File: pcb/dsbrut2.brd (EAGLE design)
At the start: 51.6 x 38 mm, 13 parts, among them IC1 4175D, IC2 74HC125D, IC3 MEGA8-AI

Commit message: added fuse, fixed ic1 power supply with VSS
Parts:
- added L1: INDUCTOR-L1812, dp_devices:L1812
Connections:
- removed net VSS: IC1.8
- new net N$1: L1.2, U$1.P$1
- net +3V3: now also L1.1; no longer U$1.P$1
- net GND: now also IC1.8
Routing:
- net +3V3: track 85.7 -> 66.2 mm
- net N$1: track 0.00 -> 18.7 mm
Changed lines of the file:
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@@
 <layer number="24" name="bOrigins" color="15" fill="1" visible="yes" active="yes"/>
 <layer number="25" name="tNames" color="7" fill="1" visible="yes" active="yes"/>
-<layer number="26" name="bNames" color="7" fill="1" visible="no" active="yes"/>
-<layer number="27" name="tValues" color="7" fill="1" visible="no" active="yes"/>
-<layer number="28" name="bValues" color="7" fill="1" visible="no" active="yes"/>
-<layer number="29" name="tStop" color="7" fill="3" visible="no" active="yes"/>
-<layer number="30" name="bStop" color="7" fill="6" visible="no" active="yes"/>
-<layer number="31" name="tCream" color="7" fill="4" visible="no" active="yes"/>
-<layer number="32" name="bCream" color="7" fill="5" visible="no" active="yes"/>
-<layer number="33" name="tFinish" color="6" fill="3" visible="no" active="yes"/>
-<layer number="34" name="bFinish" color="6" fill="6" visible="no" active="yes"/>
-<layer number="35" name="tGlue" color="7" fill="4" visible="no" active="yes"/>
-<layer number="36" name="bGlue" color="7" fill="5" visible="no" active="yes"/>
-<layer number="37" name="tTest" color="7" fill="1" visible="no" active="yes"/>
-<layer number="38" name="bTest" color="7" fill="1" visible="no" active="yes"/>
-<layer number="39" name="tKeepout" color="4" fill="11" visible="no" active="yes"/>
+<layer number="26" name="bNames" color="7" fill="1" visible="yes" active="yes"/>
+<layer number="27" name="tValues" color="7" fill="1" visible="yes" active="yes"/>
+<layer number="28" name="bValues" color="7" fill="1" visible="yes" active="yes"/>
+<layer number="29" name="tStop" color="7" fill="3" visible="yes" active="yes"/>
+<layer number="30" name="bStop" color="7" fill="6" visible="yes" active="yes"/>
+<layer number="31" name="tCream" color="7" fill="4" visible="yes" active="yes"/>
+<layer number="32" name="bCream" color="7" fill="5" visible="yes" active="yes"/>
+<layer number="33" name="tFinish" color="6" fill="3" visible="yes" active="yes"/>
+<layer number="34" name="bFinish" color="6" fill="6" visible="yes" active="yes"/>
+<layer number="35" name="tGlue" color="7" fill="4" visible="yes" active="yes"/>
+<layer number="36" name="bGlue" color="7" fill="5" visible="yes" active="yes"/>
+<layer number="37" name="tTest" color="7" fill="1" visible="yes" active="yes"/>
+<layer number="38" name="bTest" color="7" fill="1" visible="yes" active="yes"/>
+<layer number="39" name="tKeepout" color="4" fill="11" visible="yes" active="yes"/>
 <layer number="40" name="bKeepout" color="1" fill="11" visible="yes" active="yes"/>
-<layer number="41" name="tRestrict" color="4" fill="10" visible="no" active="yes"/>
+<layer number="41" name="tRestrict" color="4" fill="10" visible="yes" active="yes"/>
 <layer number="42" name="bRestrict" color="1" fill="10" visible="yes" active="yes"/>
-<layer number="43" name="vRestrict" color="2" fill="10" visible="no" active="yes"/>
-<layer number="44" name="Drills" color="7" fill="1" visible="no" active="yes"/>
-<layer number="45" name="Holes" color="7" fill="1" visible="no" active="yes"/>
-<layer number="46" name="Milling" color="3" fill="1" visible="no" active="yes"/>
-<layer number="47" name="Measures" color="7" fill="1" visible="no" active="yes"/>
-<layer number="48" name="Document" color="7" fill="1" visible="no" active="yes"/>
-<layer number="49" name="Reference" color="7" fill="1" visible="no" active="yes"/>
+<layer number="43" name="vRestrict" color="2" fill="10" visible="yes" active="yes"/>
+<layer number="44" name="Drills" color="7" fill="1" visible="yes" active="yes"/>
+<layer number="45" name="Holes" color="7" fill="1" visible="yes" active="yes"/>
+<layer number="46" name="Milling" color="3" fill="1" visible="yes" active="yes"/>
+<layer number="47" name="Measures" color="7" fill="1" visible="yes" active="yes"/>
+<layer number="48" name="Document" color="7" fill="1" visible="yes" active="yes"/>
+<layer number="49" name="Reference" color="7" fill="1" visible="yes" active="yes"/>
 <layer number="50" name="dxf" color="7" fill="1" visible="no" active="no"/>
-<layer number="51" name="tDocu" color="7" fill="1" visible="no" active="yes"/>
-<layer number="52" name="bDocu" color="7" fill="1" visible="no" active="yes"/>
+<layer number="51" name="tDocu" color="7" fill="1" visible="yes" active="yes"/>
+<layer number="52" name="bDocu" color="7" fill="1" visible="yes" active="yes"/>
 <layer number="53" name="tGND_GNDA" color="7" fill="9" visible="no" active="no"/>
 <layer number="54" name="bGND_GNDA" color="1" fill="9" visible="no" active="no"/>
@@
 <layer number="98" name="Guide" color="6" fill="1" visible="no" active="no"/>
 <layer number="100" name="Muster" color="7" fill="1" visible="no" active="no"/>
-<layer number="101" name="Patch_Top" color="12" fill="4" visible="no" active="yes"/>
-<layer number="102" name="Vscore" color="7" fill="1" visible="no" active="yes"/>
+<layer number="101" name="Patch_Top" color="12" fill="4" visible="yes" active="yes"/>
+<layer number="102" name="Vscore" color="7" fill="1" visible="yes" active="yes"/>
 <layer number="103" name="tMap" color="7" fill="1" visible="no" active="yes"/>
 <layer number="104" name="Name" color="16" fill="1" visible="no" active="yes"/>
@@
 <attribute name="VALUE" x="48.41875" y="14.76375" size="1.27" layer="27" rot="R90"/>
 </element>
+<element name="L1" library="dp_devices" package="L1812" value="INDUCTOR-L1812" x="2.69875" y="22.70125" rot="R270"/>
 </elements>
 <signals>
-<signal name="VSS">
-<contactref element="IC1" pad="8"/>
-</signal>
 <signal name="VDD">
 <contactref element="IC1" pad="16"/>
@@
 </polygon>
 <polygon width="0.4064" layer="16" isolate="0.3048">
-<vertex x="-1.905" y="-1.27"/>
-<vertex x="51.435" y="-1.27"/>
+<vertex x="-2.2225" y="6.35"/>
+<vertex x="51.1175" y="6.35"/>
 <vertex x="51.435" y="40.005"/>
 <vertex x="-1.905" y="40.005"/>
@@
 <via x="17.62125" y="29.68625" extent="1-16" drill="0.8"/>
 <via x="15.875" y="7.9375" extent="1-16" drill="0.8" diameter="0.8128"/>
+<contactref element="IC1" pad="8"/>
 </signal>
 <signal name="+3V3">
 <contactref element="JP1" pad="1"/>
 <contactref element="IC1" pad="1"/>
-<contactref element="U$1" pad="P$1"/>
 <contactref element="IC3" pad="6"/>
 <contactref element="IC3" pad="4"/>
 <contactref element="TP1" pad="TP"/>
 <contactref element="IC2" pad="14"/>
-<wire x1="1.0406375" y1="3.32515" x2="1.0406375" y2="12.4706375" width="0.8128" layer="1"/>
-<wire x1="1.0406375" y1="12.4706375" x2="3.175" y2="14.2875" width="0.8128" layer="1"/>
-<wire x1="3.175" y1="14.2875" x2="3.175" y2="22.5425" width="0.8128" layer="1"/>
-<wire x1="3.175" y1="22.5425" x2="3.4925" y2="22.86" width="0.8128" layer="1"/>
-<wire x1="3.4925" y1="22.86" x2="6.4516" y2="22.86" width="0.8128" layer="1"/>
 <wire x1="33.8074" y1="16.58" x2="34.995" y2="16.58" width="0.4064" layer="1"/>
 <wire x1="34.995" y1="16.58" x2="35.56" y2="17.145" width="0.6096" layer="1"/>
@@
 <wire x1="26.5684" y1="21.59" x2="25.710128125" y2="21.58388125" width="0.8128" layer="1"/>
 <wire x1="15.875" y1="32.7025" x2="15.686540625" y2="34.56710625" width="0.8128" layer="1"/>
-<wire x1="6.4516" y1="22.86" x2="6.4516" y2="24.2316" width="0.8128" layer="1"/>
-<wire x1="6.4516" y1="24.2316" x2="8.89" y2="26.67" width="0.8128" layer="1"/>
-<wire x1="8.89" y1="26.67" x2="14.605" y2="26.67" width="0.8128" layer="1"/>
+<wire x1="8.73125" y1="26.67" x2="14.605" y2="26.67" width="0.8128" layer="1"/>
 <wire x1="26.5684" y1="21.59" x2="28.2575" y2="21.59" width="0.8128" layer="1"/>
 <wire x1="28.2575" y1="21.59" x2="31.75" y2="18.0975" width="0.8128" layer="1"/>
@@
 <wire x1="43.815" y1="16.1925" x2="43.815" y2="16.8275" width="0.4064" layer="1"/>
 <wire x1="43.815" y1="16.8275" x2="43.2625" y2="17.38" width="0.4064" layer="1"/>
+<contactref element="L1" pad="1"/>
+<wire x1="8.73125" y1="26.67" x2="6.50875" y2="24.4475" width="0.8128" layer="1"/>
+<wire x1="6.50875" y1="24.4475" x2="6.50875" y2="23.97125" width="0.8128" layer="1"/>
+<wire x1="6.50875" y1="23.97125" x2="6.50875" y2="22.91715" width="0.8128" layer="1"/>
+<wire x1="6.50875" y1="22.91715" x2="6.4516" y2="22.86" width="0.8128" layer="1"/>
+<wire x1="2.69875" y1="24.30125" x2="6.3625" y2="24.30125" width="0.8128" layer="1"/>
+<wire x1="6.3625" y1="24.30125" x2="6.50875" y2="23.97125" width="0.8128" layer="1"/>
 </signal>
 <signal name="PD1">
@@
 <wire x1="45.87875" y1="16.98375" x2="45.87875" y2="18.6175" width="0.4064" layer="1"/>
 </signal>
+<signal name="N$1">
+<contactref element="U$1" pad="P$1"/>
+<contactref element="L1" pad="2"/>
+<wire x1="2.69875" y1="21.10125" x2="2.69875" y2="19.685" width="0.8128" layer="1"/>
+<wire x1="2.69875" y1="19.685" x2="3.01625" y2="19.20875" width="0.8128" layer="1"/>
+<wire x1="3.01625" y1="19.20875" x2="3.01625" y2="15.39875" width="0.8128" layer="1"/>
+<wire x1="3.01625" y1="15.39875" x2="1.11125" y2="13.49375" width="0.8128" layer="1"/>
+<wire x1="1.11125" y1="13.49375" x2="1.11125" y2="3.3957625" width="0.8128" layer="1"/>
+<wire x1="1.11125" y1="3.3957625" x2="1.0406375" y2="3.32515" width="0.8128" layer="1"/>
+</signal>
 </signals>

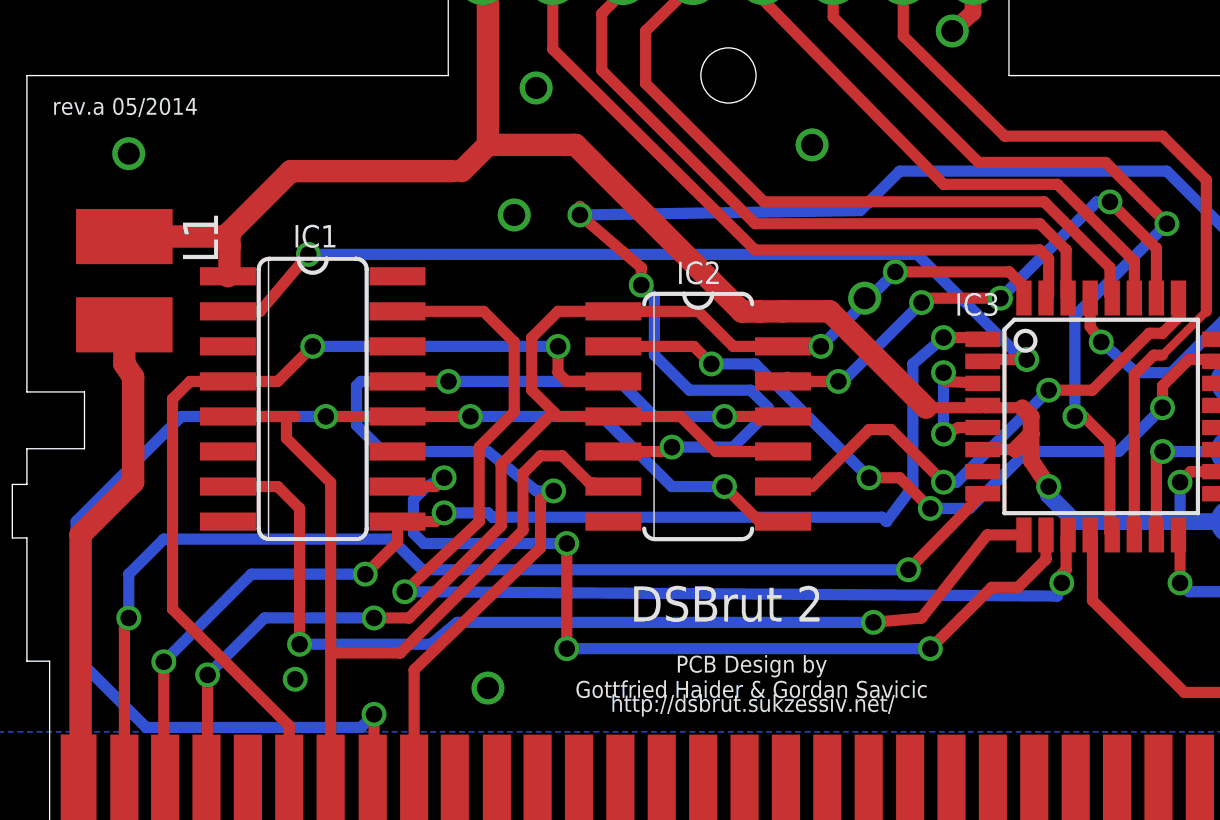
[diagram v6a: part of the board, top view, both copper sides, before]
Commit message: Changed fuse label, moved a via, minor trace beautification
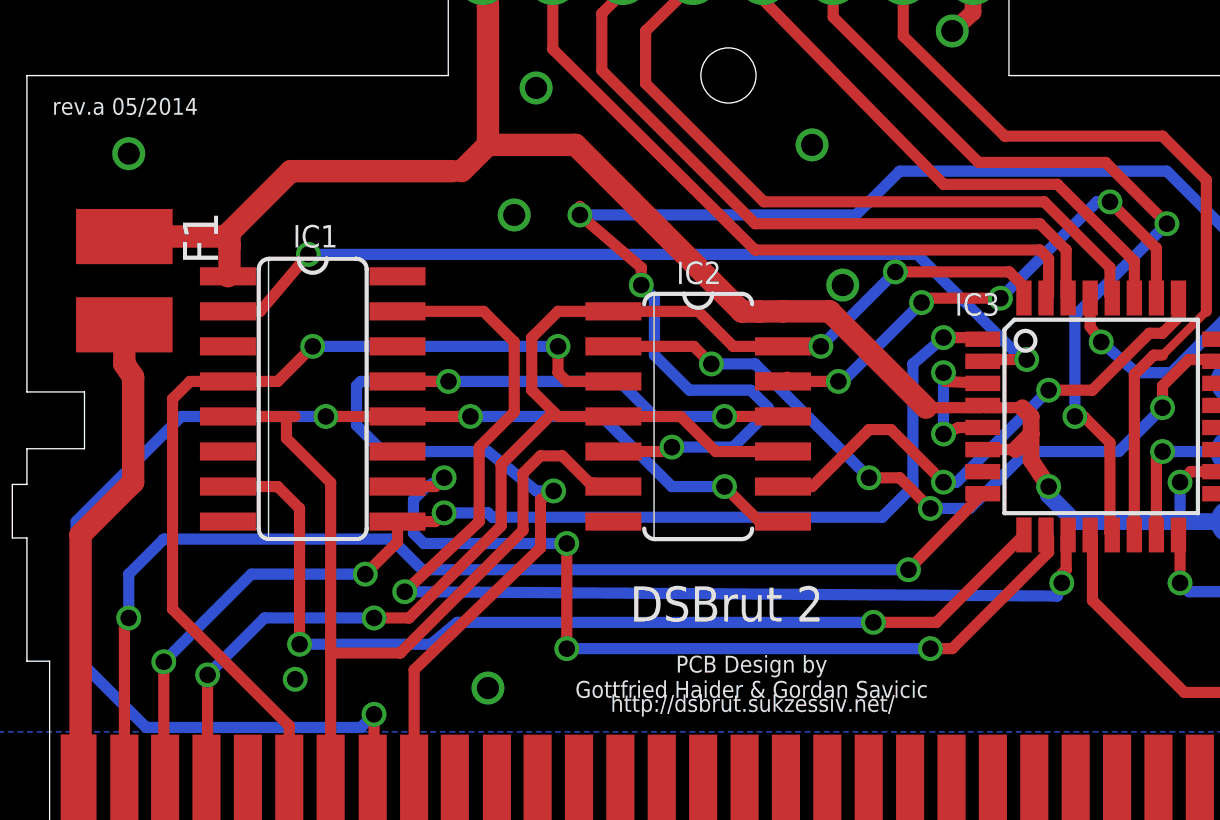
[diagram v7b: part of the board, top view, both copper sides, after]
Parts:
- F1: value INDUCTOR-L1812 -> F1
- renumbered L1 to F1
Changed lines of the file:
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@@
 <attribute name="VALUE" x="48.41875" y="14.76375" size="1.27" layer="27" rot="R90"/>
 </element>
-<element name="L1" library="dp_devices" package="L1812" value="INDUCTOR-L1812" x="2.69875" y="22.70125" rot="R270"/>
+<element name="F1" library="dp_devices" package="L1812" value="F1" x="2.69875" y="22.70125" smashed="yes" rot="R270">
+<attribute name="NAME" x="4.82375" y="25.20125" size="1.27" layer="25" font="vector" ratio="10" rot="R270"/>
+<attribute name="VALUE" x="-0.04125" y="23.61375" size="0.8128" layer="27" font="vector" ratio="10" rot="R270"/>
+</element>
 </elements>
 <signals>
@@
 <wire x1="47.8156375" y1="6.1593625" x2="45.085" y2="8.89" width="0.4064" layer="1"/>
 <via x="16.8275" y="25.0825" extent="1-16" drill="0.8"/>
-<via x="29.5275" y="22.06625" extent="1-16" drill="0.8"/>
+<via x="28.73375" y="22.5425" extent="1-16" drill="0.8"/>
 <via x="2.8575" y="27.305" extent="1-16" drill="0.8"/>
 <via x="27.6225" y="27.6225" extent="1-16" drill="0.8"/>
@@
 <wire x1="43.815" y1="16.1925" x2="43.815" y2="16.8275" width="0.4064" layer="1"/>
 <wire x1="43.815" y1="16.8275" x2="43.2625" y2="17.38" width="0.4064" layer="1"/>
-<contactref element="L1" pad="1"/>
+<contactref element="F1" pad="1"/>
 <wire x1="8.73125" y1="26.67" x2="6.50875" y2="24.4475" width="0.8128" layer="1"/>
 <wire x1="6.50875" y1="24.4475" x2="6.50875" y2="23.97125" width="0.8128" layer="1"/>
@@
 <contactref element="IC1" pad="7"/>
 <contactref element="IC3" pad="9"/>
-<wire x1="35.3" y1="13.4874" x2="33.96615" y2="13.4874" width="0.4064" layer="1"/>
-<wire x1="33.96615" y1="13.4874" x2="31.59125" y2="10.4775" width="0.4064" layer="1"/>
-<wire x1="31.59125" y1="10.4775" x2="29.845" y2="10.31875" width="0.4064" layer="1"/>
 <via x="29.845" y="10.31875" extent="1-16" drill="0.6"/>
 <wire x1="29.845" y1="10.31875" x2="14.76375" y2="10.31875" width="0.4064" layer="16"/>
@@
 <wire x1="9.04875" y1="14.44625" x2="8.255" y2="15.24" width="0.4064" layer="1"/>
 <wire x1="8.255" y1="15.24" x2="6.4516" y2="15.24" width="0.4064" layer="1"/>
+<wire x1="29.845" y1="10.31875" x2="32.13135" y2="10.31875" width="0.4064" layer="1"/>
+<wire x1="32.13135" y1="10.31875" x2="35.3" y2="13.4874" width="0.4064" layer="1"/>
 </signal>
 <signal name="WR">
@@
 <wire x1="32.385" y1="20.6375" x2="33.7499" y2="20.6375" width="0.4064" layer="1"/>
 <wire x1="33.7499" y1="20.6375" x2="33.8074" y2="20.58" width="0.4064" layer="1"/>
-<wire x1="30.32125" y1="13.97" x2="31.27375" y2="15.24" width="0.4064" layer="16"/>
 <wire x1="14.2875" y1="14.2875" x2="15.875" y2="14.2875" width="0.4064" layer="16"/>
 <wire x1="15.875" y1="14.2875" x2="16.03375" y2="14.12875" width="0.4064" layer="16"/>
 <wire x1="16.03375" y1="14.12875" x2="30.1625" y2="14.12875" width="0.4064" layer="16"/>
-<wire x1="30.1625" y1="14.12875" x2="30.32125" y2="13.97" width="0.4064" layer="16"/>
 <wire x1="12.5984" y1="13.97" x2="13.97" y2="13.97" width="0.4064" layer="1"/>
 <wire x1="13.97" y1="13.97" x2="14.2875" y2="14.2875" width="0.4064" layer="1"/>
 <wire x1="4.1275" y1="8.89" x2="7.3025" y2="12.065" width="0.4064" layer="16"/>
 <wire x1="7.3025" y1="12.065" x2="11.43" y2="12.065" width="0.4064" layer="16"/>
+<wire x1="30.1625" y1="14.12875" x2="31.27375" y2="15.24" width="0.4064" layer="16"/>
 </signal>
 <signal name="PD6">
 <contactref element="IC1" pad="10"/>
 <contactref element="IC3" pad="10"/>
-<wire x1="36.1" y1="13.4874" x2="36.1" y2="12.605" width="0.4064" layer="1"/>
 <wire x1="18.7325" y1="9.36625" x2="18.7325" y2="13.17625" width="0.4064" layer="1"/>
 <via x="18.7325" y="13.17625" extent="1-16" drill="0.6"/>
 <wire x1="18.7325" y1="13.17625" x2="13.5509" y2="13.17625" width="0.4064" layer="16"/>
 <via x="14.2875" y="15.5575" extent="1-16" drill="0.6"/>
-<wire x1="34.13125" y1="11.58875" x2="31.90875" y2="9.36625" width="0.4064" layer="1"/>
 <via x="31.90875" y="9.36625" extent="1-16" drill="0.6"/>
 <wire x1="31.90875" y1="9.36625" x2="18.7325" y2="9.36625" width="0.4064" layer="16"/>
 <via x="18.7325" y="9.36625" extent="1-16" drill="0.6"/>
-<wire x1="36.1" y1="12.605" x2="35.08375" y2="11.58875" width="0.4064" layer="1"/>
-<wire x1="35.08375" y1="11.58875" x2="34.13125" y2="11.58875" width="0.4064" layer="1"/>
 <wire x1="14.2875" y1="15.5575" x2="13.6525" y2="15.24" width="0.4064" layer="16"/>
 <wire x1="13.6525" y1="15.24" x2="13.17625" y2="14.76375" width="0.4064" layer="16"/>
@@
 <wire x1="12.5984" y1="15.24" x2="13.97" y2="15.24" width="0.4064" layer="1"/>
 <wire x1="13.97" y1="15.24" x2="14.2875" y2="15.5575" width="0.4064" layer="1"/>
+<wire x1="31.90875" y1="9.36625" x2="32.7025" y2="9.36625" width="0.4064" layer="1"/>
+<wire x1="32.7025" y1="9.36625" x2="36.195" y2="12.85875" width="0.4064" layer="1"/>
+<wire x1="36.195" y1="12.85875" x2="36.195" y2="13.3924" width="0.4064" layer="1"/>
+<wire x1="36.195" y1="13.3924" x2="36.1" y2="13.4874" width="0.4064" layer="1"/>
 </signal>
 <signal name="GBA8">
@@
 <wire x1="43.33875" y1="23.8125" x2="40.48125" y2="26.67" width="0.4064" layer="16"/>
 <wire x1="40.48125" y1="26.67" x2="30.7975" y2="26.67" width="0.4064" layer="16"/>
-<wire x1="30.7975" y1="26.67" x2="29.36875" y2="25.24125" width="0.4064" layer="16"/>
-<wire x1="29.36875" y1="25.24125" x2="19.20875" y2="25.0825" width="0.4064" layer="16"/>
 <wire x1="20.4216" y1="16.51" x2="22.225" y2="16.51" width="0.4064" layer="1"/>
 <wire x1="22.225" y1="16.51" x2="22.5425" y2="16.66875" width="0.4064" layer="1"/>
@@
 <wire x1="19.20875" y1="25.4" x2="19.20875" y2="25.0825" width="0.4064" layer="1"/>
 <via x="19.20875" y="25.0825" extent="1-16" drill="0.6"/>
+<wire x1="19.20875" y1="25.0825" x2="29.21" y2="25.0825" width="0.4064" layer="16"/>
+<wire x1="29.21" y1="25.0825" x2="30.7975" y2="26.67" width="0.4064" layer="16"/>
 </signal>
 <signal name="PC0">
@@
 <signal name="N$1">
 <contactref element="U$1" pad="P$1"/>
-<contactref element="L1" pad="2"/>
+<contactref element="F1" pad="2"/>
 <wire x1="2.69875" y1="21.10125" x2="2.69875" y2="19.685" width="0.8128" layer="1"/>
 <wire x1="2.69875" y1="19.685" x2="3.01625" y2="19.20875" width="0.8128" layer="1"/>
